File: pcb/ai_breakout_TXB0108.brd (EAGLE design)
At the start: 15.2 x 25.4 mm, 8 parts, among them J1 1X10, J2 1X10

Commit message: small update schematic
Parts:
- IC1: value (none) -> TXB0108
- J2: value 1X10 -> 1X10NOFIRST; device Ai_Connectors:1X10 -> Ai_Connectors:1X10-NOFIRST
- moved J1 12.7 mm to (14.0, 12.7)
- moved J2 12.7 mm to (1.27, 12.7)
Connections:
- net A1: now also J2.2; no longer J1.9
- net A2: now also J2.3; no longer J1.8
- net A3: now also J2.4; no longer J1.7
- net A4: now also J2.5; no longer J1.6
- net A5: now also J2.6; no longer J1.5
- net A6: now also J2.7; no longer J1.4
- net A7: now also J2.8; no longer J1.3
- net A8: now also J2.9; no longer J1.2
- net B1: now also J1.9; no longer J2.2
- net B2: now also J1.8; no longer J2.3
- net B3: now also J1.7; no longer J2.4
- net B4: now also J1.6; no longer J2.5
- net B5: now also J1.5; no longer J2.6
- net B6: now also J1.4; no longer J2.7
- net B7: now also J1.3; no longer J2.8
- net B8: now also J1.2; no longer J2.9
- net GND: now also J1.1; no longer J2.10
- net OE: now also J2.10; no longer J1.1
- net VCC-A: now also J2.1; no longer J1.10
- net VCC-B: now also J1.10; no longer J2.1

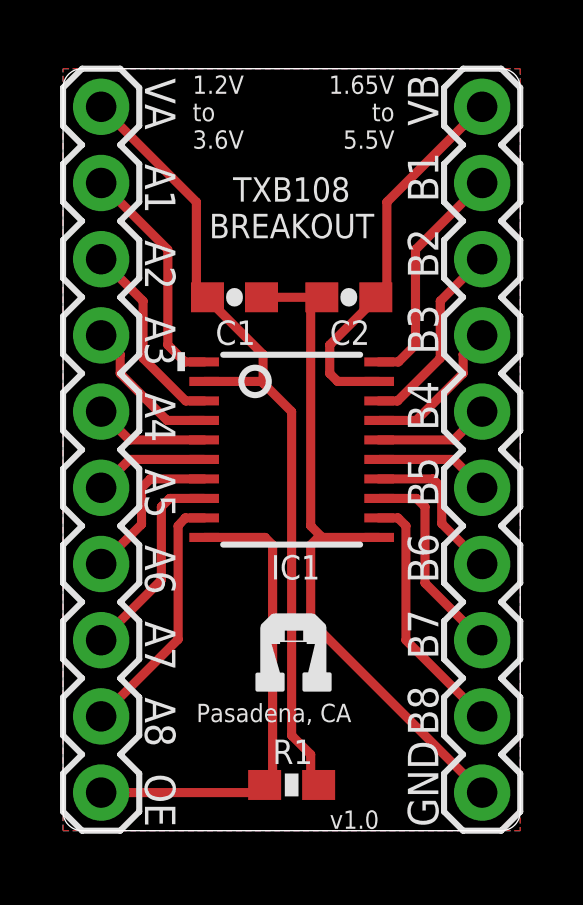
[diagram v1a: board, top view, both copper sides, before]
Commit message: adding additional licensing information
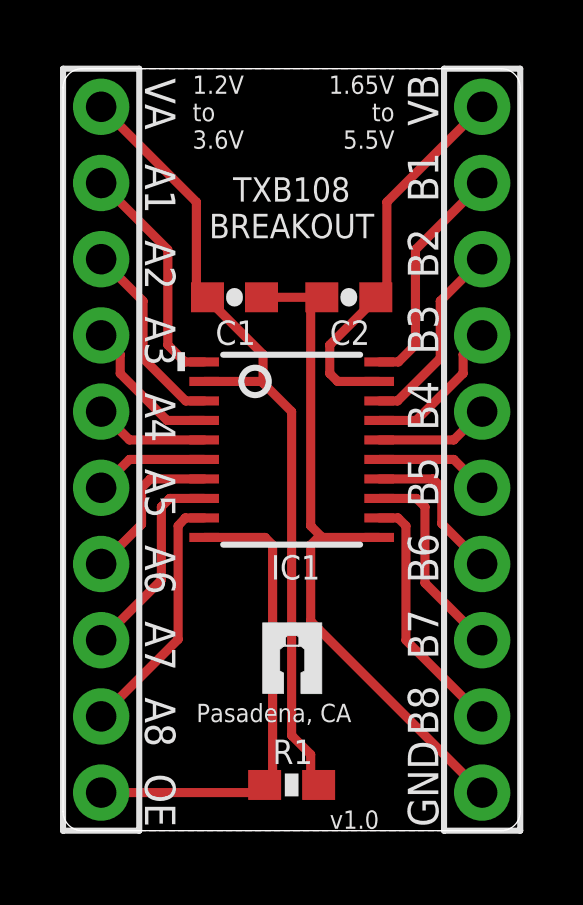
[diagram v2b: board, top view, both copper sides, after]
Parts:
- added FRAME1: FRAME-LETTER, Ai_Miscellany:CREATIVE-COMMONS
- moved U$2 0.38 mm to (8.64, 4.57)
- moved U$1 0.30 mm to (6.65, 4.57)
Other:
- board text added: "@MakerBro"
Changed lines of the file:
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@@
 <layer number="20" name="Dimension" color="15" fill="1" visible="yes" active="yes"/>
 <layer number="21" name="tPlace" color="7" fill="1" visible="yes" active="yes"/>
-<layer number="22" name="bPlace" color="7" fill="1" visible="yes" active="yes"/>
+<layer number="22" name="bPlace" color="13" fill="1" visible="yes" active="yes"/>
 <layer number="23" name="tOrigins" color="15" fill="1" visible="yes" active="yes"/>
 <layer number="24" name="bOrigins" color="15" fill="1" visible="yes" active="yes"/>
@@
 <layer number="49" name="Reference" color="7" fill="1" visible="yes" active="yes"/>
 <layer number="50" name="dxf" color="7" fill="1" visible="no" active="no"/>
-<layer number="51" name="tDocu" color="7" fill="1" visible="yes" active="yes"/>
+<layer number="51" name="tDocu" color="14" fill="1" visible="yes" active="yes"/>
 <layer number="52" name="bDocu" color="7" fill="1" visible="yes" active="yes"/>
 <layer number="53" name="tGND_GNDA" color="7" fill="9" visible="no" active="no"/>
@@
 <layer number="56" name="wert" color="7" fill="1" visible="no" active="no"/>
 <layer number="57" name="tCAD" color="7" fill="1" visible="no" active="no"/>
+<layer number="59" name="tCarbon" color="7" fill="1" visible="no" active="no"/>
+<layer number="60" name="bCarbon" color="7" fill="1" visible="no" active="no"/>
+<layer number="90" name="Modules" color="5" fill="1" visible="no" active="no"/>
 <layer number="91" name="Nets" color="2" fill="1" visible="no" active="no"/>
 <layer number="92" name="Busses" color="1" fill="1" visible="no" active="no"/>
@@
 <layer number="223" name="223bmp" color="24" fill="1" visible="no" active="no"/>
 <layer number="224" name="224bmp" color="25" fill="1" visible="no" active="no"/>
+<layer number="225" name="225bmp" color="7" fill="1" visible="yes" active="yes"/>
+<layer number="226" name="226bmp" color="7" fill="1" visible="yes" active="yes"/>
+<layer number="227" name="227bmp" color="7" fill="1" visible="yes" active="yes"/>
+<layer number="228" name="228bmp" color="7" fill="1" visible="yes" active="yes"/>
+<layer number="229" name="229bmp" color="7" fill="1" visible="yes" active="yes"/>
+<layer number="230" name="230bmp" color="7" fill="1" visible="yes" active="yes"/>
+<layer number="231" name="231bmp" color="7" fill="1" visible="yes" active="yes"/>
 <layer number="248" name="Housing" color="7" fill="1" visible="yes" active="yes"/>
 <layer number="249" name="Edge" color="7" fill="1" visible="yes" active="yes"/>
@@
 <layer number="251" name="SMDround" color="7" fill="1" visible="yes" active="yes"/>
 <layer number="254" name="cooling" color="7" fill="1" visible="yes" active="yes"/>
+<layer number="255" name="routoute" color="7" fill="1" visible="yes" active="yes"/>
 </layers>
 <board>
@@
 <text x="7.62" y="20.7645" size="0.8128" layer="21" font="vector" ratio="10" rot="SR0" align="center">TXB108
 BREAKOUT</text>
+<text x="1.27" y="-17.78" size="1.524" layer="51" font="vector" ratio="10">@MakerBro</text>
 </plain>
 <attributes>
@@
 <attribute name="NAME" x="6.985" y="2.2225" size="0.8128" layer="25" font="vector" ratio="10"/>
 </element>
-<element name="U$1" library="Ai_Miscellany" package="AI-LOGO-XS" value="AI-LOGOXS" x="6.35" y="4.572"/>
-<element name="U$2" library="Ai_Miscellany" package="AI-LOGO-XS" value="AI-LOGOXS" x="9.017" y="4.572" rot="MR0"/>
+<element name="U$1" library="Ai_Miscellany" package="AI-LOGO-XS" value="AI-LOGOXS" x="6.6548" y="4.572"/>
+<element name="U$2" library="Ai_Miscellany" package="AI-LOGO-XS" value="AI-LOGOXS" x="8.636" y="4.572" rot="MR0"/>
 <element name="J1" library="Ai_Connectors" package="1X10" value="1X10" x="13.97" y="12.7" smashed="yes" rot="R90"/>
 <element name="J2" library="Ai_Connectors" package="1X10-NOFIRST" value="1X10NOFIRST" x="1.27" y="12.7" smashed="yes" rot="R270"/>
+<element name="FRAME1" library="Ai_Miscellany" package="CREATIVE-COMMONS" value="FRAME-LETTER" x="7.62" y="-1.27">
+<attribute name="REV" value="1.0" x="7.62" y="-1.27" size="1.778" layer="27" display="off"/>
+</element>
 </elements>
 <signals>
